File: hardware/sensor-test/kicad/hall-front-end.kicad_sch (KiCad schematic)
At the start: 29 parts, among them U4 TPS22919DCKR, U5 TMUX1208PWR, U6 DRV5055A3QDBZR, U7 DRV5055A3QDBZR, U8 DRV5055A3QDBZR, U9 DRV5055A3QDBZR

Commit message: Correct Hall front-end pin mapping and ERC sources
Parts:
- added X1: RP2040 control outputs (logical placeholder), symbol HEP:ExternalController
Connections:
- net GND: now also U4.2 (GND), U5.14 (GND), U6.3 (GND), U7.3 (GND), U8.3 (GND), U9.3 (GND); no longer U5.13 (VDD), U6.1 (VCC), U7.1 (VCC), U8.1 (VCC), U9.1 (VCC)
- net H0_RAW: now also U5.4 (S1); no longer U5.10 (S7)
- net H1_RAW: now also U5.5 (S2); no longer U5.12 (S5)
- net H2_RAW: now also TP6.1, U9.2 (OUT)
- net HALL_5V: now also U4.6 (OUT), U5.13 (VDD), U6.1 (VCC), U7.1 (VCC), U8.1 (VCC), U9.1 (VCC); no longer U4.4 (NC), U4.5 (QOD), U5.14 (GND), U6.3 (GND), U7.3 (GND), U8.3 (GND), U9.3 (GND)
- net HALL_PWR_EN: now also X1.1 (HALL_PWR_EN)
- net MUX_A0: now also U5.1 (A0), X1.2 (MUX_A0)
- net MUX_A1: now also U5.16 (A1), X1.3 (MUX_A1)
- net MUX_A2: now also X1.4 (MUX_A2)
- net MUX_D: now also U5.8 (D)
- net MUX_EN0: now also U5.2 (EN), X1.5 (MUX_EN0)
- net MUX_S5_SPARE: now also U5.12 (S5); no longer U5.5 (S2)
- net MUX_S6_SPARE: now also U5.11 (S6)
- net MUX_S7_SPARE: now also U5.10 (S7); no longer U5.4 (S1)
- net MUX_S8_SPARE: now also U5.9 (S8)
- net VBUS: now also U4.1 (IN)
- removed net H3_RAW: TP6.1, U5.6 (S3), U9.2 (OUT)
- no-connect marks 2 -> 3
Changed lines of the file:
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@@
     (company "HE Piantor 42")
   )
-(no_connect (at 53.89 39.92))
+(no_connect (at 53.89 50.08))
+  (no_connect (at 53.89 45))
   (no_connect (at 142.7 89.76))
-(label "VBUS" (at 36.11 50.08 0)
+(label "VBUS" (at 36.11 39.92 0)
     (effects (font (size 1.27 1.27)) (justify left bottom))
   )
@@
     (effects (font (size 1.27 1.27)) (justify left bottom))
   )
-  (label "GND" (at 45 34.84 0)
-    (effects (font (size 1.27 1.27)) (justify left bottom))
-  )
-  (label "HALL_5V" (at 53.89 45 0)
-    (effects (font (size 1.27 1.27)) (justify left bottom))
-  )
-  (label "HALL_5V" (at 53.89 50.08 0)
-    (effects (font (size 1.27 1.27)) (justify left bottom))
-  )
-  (label "HALL_5V" (at 130 125.32 0)
-    (effects (font (size 1.27 1.27)) (justify left bottom))
-  )
-  (label "GND" (at 130 84.68 0)
-    (effects (font (size 1.27 1.27)) (justify left bottom))
-  )
-  (label "MUX_A0" (at 142.7 110.08 0)
-    (effects (font (size 1.27 1.27)) (justify left bottom))
-  )
-  (label "MUX_A1" (at 142.7 107.54 0)
+  (label "GND" (at 45 55.16 0)
+    (effects (font (size 1.27 1.27)) (justify left bottom))
+  )
+  (label "HALL_5V" (at 53.89 39.92 0)
+    (effects (font (size 1.27 1.27)) (justify left bottom))
+  )
+  (label "HALL_5V" (at 130 84.68 0)
+    (effects (font (size 1.27 1.27)) (justify left bottom))
+  )
+  (label "GND" (at 130 125.32 0)
+    (effects (font (size 1.27 1.27)) (justify left bottom))
+  )
+  (label "MUX_A0" (at 142.7 99.92 0)
+    (effects (font (size 1.27 1.27)) (justify left bottom))
+  )
+  (label "MUX_A1" (at 142.7 102.46 0)
     (effects (font (size 1.27 1.27)) (justify left bottom))
   )
@@
     (effects (font (size 1.27 1.27)) (justify left bottom))
   )
-  (label "MUX_EN0" (at 142.7 97.38 0)
-    (effects (font (size 1.27 1.27)) (justify left bottom))
-  )
-  (label "MUX_D" (at 142.7 117.7 0)
-    (effects (font (size 1.27 1.27)) (justify left bottom))
-  )
-  (label "H0_RAW" (at 117.3 117.7 0)
-    (effects (font (size 1.27 1.27)) (justify left bottom))
-  )
-  (label "H1_RAW" (at 117.3 112.62 0)
+  (label "MUX_EN0" (at 142.7 112.62 0)
+    (effects (font (size 1.27 1.27)) (justify left bottom))
+  )
+  (label "MUX_D" (at 142.7 92.3 0)
+    (effects (font (size 1.27 1.27)) (justify left bottom))
+  )
+  (label "H0_RAW" (at 117.3 92.3 0)
+    (effects (font (size 1.27 1.27)) (justify left bottom))
+  )
+  (label "H1_RAW" (at 117.3 97.38 0)
     (effects (font (size 1.27 1.27)) (justify left bottom))
   )
@@
     (effects (font (size 1.27 1.27)) (justify left bottom))
   )
-  (label "H3_RAW" (at 117.3 102.46 0)
-    (effects (font (size 1.27 1.27)) (justify left bottom))
-  )
-  (label "HALL_5V" (at 55 97.62 0)
+  (label "H3_RAW" (at 117.3 107.54 0)
+    (effects (font (size 1.27 1.27)) (justify left bottom))
+  )
+  (label "HALL_5V" (at 55 82.38 0)
     (effects (font (size 1.27 1.27)) (justify left bottom))
   )
@@
     (effects (font (size 1.27 1.27)) (justify left bottom))
   )
-  (label "GND" (at 55 82.38 0)
-    (effects (font (size 1.27 1.27)) (justify left bottom))
-  )
-  (label "HALL_5V" (at 55 125.62 0)
+  (label "GND" (at 55 97.62 0)
+    (effects (font (size 1.27 1.27)) (justify left bottom))
+  )
+  (label "HALL_5V" (at 55 110.38 0)
     (effects (font (size 1.27 1.27)) (justify left bottom))
   )
@@
     (effects (font (size 1.27 1.27)) (justify left bottom))
   )
-  (label "GND" (at 55 110.38 0)
-    (effects (font (size 1.27 1.27)) (justify left bottom))
-  )
-  (label "HALL_5V" (at 55 153.62 0)
+  (label "GND" (at 55 125.62 0)
+    (effects (font (size 1.27 1.27)) (justify left bottom))
+  )
+  (label "HALL_5V" (at 55 138.38 0)
     (effects (font (size 1.27 1.27)) (justify left bottom))
   )
@@
     (effects (font (size 1.27 1.27)) (justify left bottom))
   )
-  (label "GND" (at 55 138.38 0)
-    (effects (font (size 1.27 1.27)) (justify left bottom))
-  )
-  (label "HALL_5V" (at 55 181.62 0)
+  (label "GND" (at 55 153.62 0)
+    (effects (font (size 1.27 1.27)) (justify left bottom))
+  )
+  (label "HALL_5V" (at 55 166.38 0)
     (effects (font (size 1.27 1.27)) (justify left bottom))
   )
@@
     (effects (font (size 1.27 1.27)) (justify left bottom))
   )
-  (label "GND" (at 55 166.38 0)
+  (label "GND" (at 55 181.62 0)
     (effects (font (size 1.27 1.27)) (justify left bottom))
   )
@@
     (effects (font (size 1.27 1.27)) (justify left bottom))
   )
-  (label "MUX_S5_SPARE" (at 117.3 97.38 0)
-    (effects (font (size 1.27 1.27)) (justify left bottom))
-  )
-  (label "MUX_S6_SPARE" (at 117.3 94.84 0)
-    (effects (font (size 1.27 1.27)) (justify left bottom))
-  )
-  (label "MUX_S7_SPARE" (at 117.3 92.3 0)
-    (effects (font (size 1.27 1.27)) (justify left bottom))
-  )
-  (label "MUX_S8_SPARE" (at 117.3 89.76 0)
+  (label "MUX_S5_SPARE" (at 117.3 112.62 0)
+    (effects (font (size 1.27 1.27)) (justify left bottom))
+  )
+  (label "MUX_S6_SPARE" (at 117.3 115.16 0)
+    (effects (font (size 1.27 1.27)) (justify left bottom))
+  )
+  (label "MUX_S7_SPARE" (at 117.3 117.7 0)
+    (effects (font (size 1.27 1.27)) (justify left bottom))
+  )
+  (label "MUX_S8_SPARE" (at 117.3 120.24 0)
     (effects (font (size 1.27 1.27)) (justify left bottom))
   )
@@
     (effects (font (size 1.27 1.27)) (justify left bottom))
   )
-  (sheet_instances
+(symbol (lib_id "HEP:ExternalController") (at 300 100 0) (unit 1)
+    (in_bom no) (on_board no) (dnp no)
+    (property "Reference" "X1" (at 294.92 89.84 0) (effects (font (size 1.27 1.27))))
+    (property "Value" "RP2040 control outputs (logical placeholder)" (at 305.08 89.84 0) (effects (font (size 1.27 1.27)) (justify right)))
+    (property "Footprint" "" (at 300 100 0) (effects (font (size 1.27 1.27)) hide))
+    (property "Datasheet" "~" (at 300 100 0) (effects (font (size 1.27 1.27)) hide))
+    (pin "1")
+    (pin "2")
+    (pin "3")
+    (pin "4")
+    (pin "5")
+    (instances
+      (project "hall-front-end"
+        (path "/a1000000-0000-0000-0000-000000000001"
+          (reference "X1") (unit 1)
+        )
+      )
+    )
+  )
+  (label "HALL_PWR_EN" (at 292.38 94.92 0) (effects (font (size 1.27 1.27)) (justify left bottom)))
+  (label "MUX_A0" (at 292.38 97.46 0) (effects (font (size 1.27 1.27)) (justify left bottom)))
+  (label "MUX_A1" (at 292.38 100 0) (effects (font (size 1.27 1.27)) (justify left bottom)))
+  (label "MUX_A2" (at 292.38 102.54 0) (effects (font (size 1.27 1.27)) (justify left bottom)))
+  (label "MUX_EN0" (at 292.38 105.08 0) (effects (font (size 1.27 1.27)) (justify left bottom)))
+  (symbol (lib_id "power:PWR_FLAG") (at 280 40 0) (unit 1)
+    (in_bom yes) (on_board yes) (dnp no)
+    (property "Reference" "#FLG03" (at 280 41.905 0) (effects (font (size 1.27 1.27)) hide))
+    (property "Value" "PWR_FLAG" (at 280 43.81 0) (effects (font (size 1.27 1.27))))
+    (property "Footprint" "" (at 280 40 0) (effects (font (size 1.27 1.27)) hide))
+    (property "Datasheet" "~" (at 280 40 0) (effects (font (size 1.27 1.27)) hide))
+    (pin "1")
+    (instances (project "hall-front-end" (path "/a1000000-0000-0000-0000-000000000001" (reference "#FLG03") (unit 1))))
+  )
+  (label "VBUS" (at 280 40 0) (effects (font (size 1.27 1.27)) (justify left bottom)))
+  (symbol (lib_id "power:PWR_FLAG") (at 280 52 0) (unit 1)
+    (in_bom yes) (on_board yes) (dnp no)
+    (property "Reference" "#FLG04" (at 280 53.905 0) (effects (font (size 1.27 1.27)) hide))
+    (property "Value" "PWR_FLAG" (at 280 55.81 0) (effects (font (size 1.27 1.27))))
+    (property "Footprint" "" (at 280 52 0) (effects (font (size 1.27 1.27)) hide))
+    (property "Datasheet" "~" (at 280 52 0) (effects (font (size 1.27 1.27)) hide))
+    (pin "1")
+    (instances (project "hall-front-end" (path "/a1000000-0000-0000-0000-000000000001" (reference "#FLG04") (unit 1))))
+  )
+  (label "GND" (at 280 52 0) (effects (font (size 1.27 1.27)) (justify left bottom)))
+    (sheet_instances
     (path "/" (page "1"))
   )

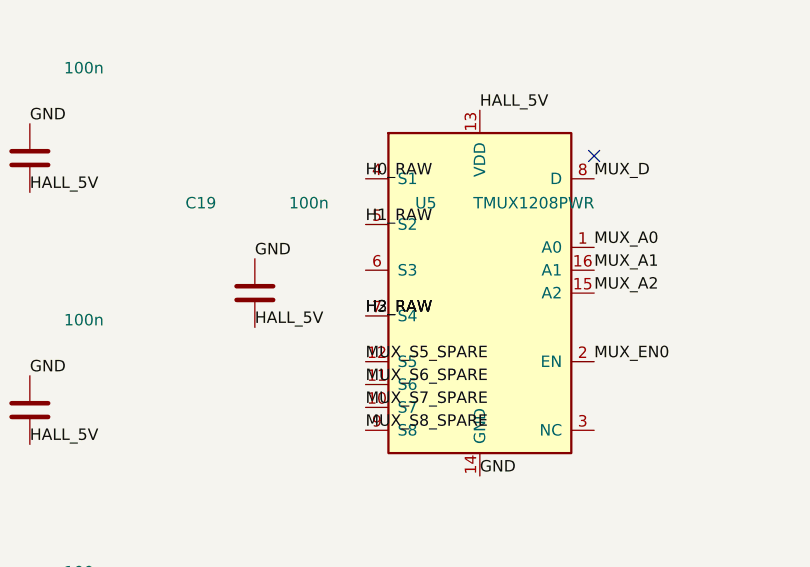
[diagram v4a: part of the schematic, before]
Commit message: Fix Hall channel 2 mux input mapping
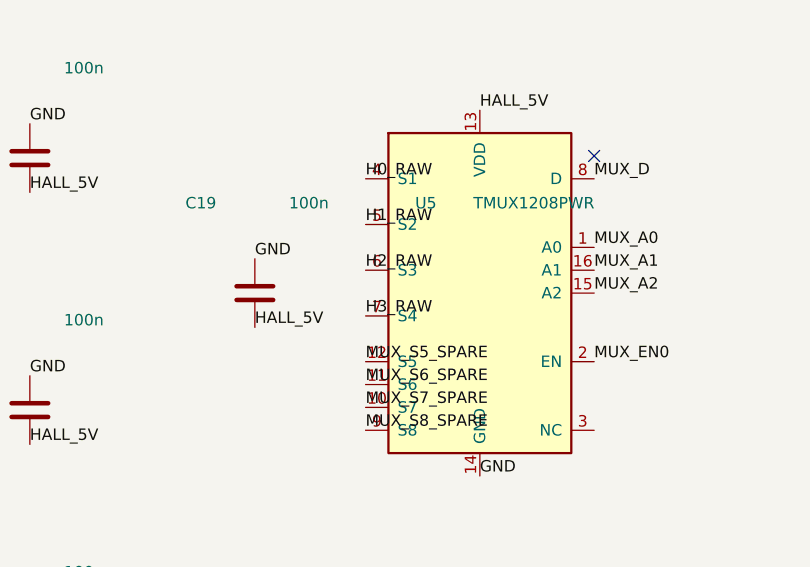
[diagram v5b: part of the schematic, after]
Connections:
- net H2_RAW: now also U5.6 (S3); no longer TP6.1, U5.7 (S4), U9.2 (OUT)
- new net H3_RAW: TP6.1, U5.7 (S4), U9.2 (OUT)
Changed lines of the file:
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@@
     (effects (font (size 1.27 1.27)) (justify left bottom))
   )
-  (label "H2_RAW" (at 117.3 107.54 0)
+  (label "H2_RAW" (at 117.3 102.46 0)
     (effects (font (size 1.27 1.27)) (justify left bottom))
   )
